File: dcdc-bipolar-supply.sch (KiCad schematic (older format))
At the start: 13 parts

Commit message: swap LT1930A for LT1930 in DCDC bipolar supply
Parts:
- removed U?: LT1930A, Package_SO:MSOP-10_3x3mm_P0.5mm, symbol linear_technology:LT1930A
- added U?: LT1930, Package_SO:MSOP-10_3x3mm_P0.5mm, symbol linear_technology:LT1930
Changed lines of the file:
@@
 Comment4 ""
 $EndDescr
-$Comp
-L linear_technology:LT1930A U?
-U 1 1 5C903C18
-P 4350 3450
-F 0 "U?" H 4350 3600 50  0000 L CNN
-F 1 "LT1930A" H 4200 3500 50  0000 L CNN
-F 2 "Package_SO:MSOP-10_3x3mm_P0.5mm" H 4350 2850 50  0001 C CNN
-F 3 "https://cds.linear.com/docs/en/datasheet/1930a.pdf" H 4450 3400 50  0001 C CNN
-	1    4350 3450
-	1    0    0    -1
-$EndComp
 Text HLabel 3200 3050 0    50   Input ~ 0
 5V_IN
@@
 Connection ~ 3300 3050
 Connection ~ 3700 3050
+$Comp
+L linear_technology:LT1930 U?
+U 1 1 5C87A250
+P 4350 3450
+F 0 "U?" H 4350 3500 50  0000 C CNN
+F 1 "LT1930" H 4350 3600 50  0000 C CNN
+F 2 "Package_SO:MSOP-10_3x3mm_P0.5mm" H 4350 2850 50  0001 C CNN
+F 3 "https://cds.linear.com/docs/en/datasheet/1930a.pdf" H 4450 3400 50  0001 C CNN
+	1    4350 3450
+	1    0    0    -1
+$EndComp
 $EndSCHEMATC

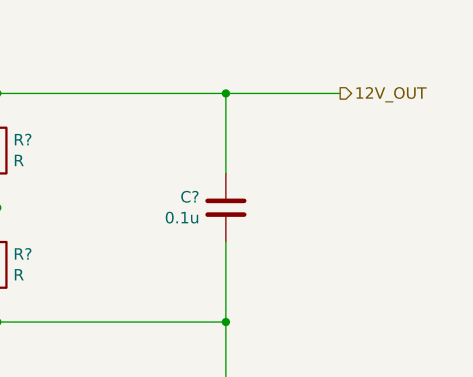
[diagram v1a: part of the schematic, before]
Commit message: add sheets for +/-12V LDOs
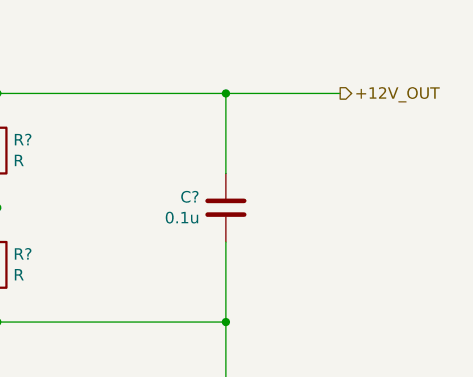
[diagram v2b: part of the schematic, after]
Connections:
- net 12V_OUT renamed +12V_OUT
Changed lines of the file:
@@
 $Descr A4 11693 8268
 encoding utf-8
-Sheet 3 3
+Sheet 3 5
 Title ""
 Date ""
@@
 Connection ~ 6500 3550
 Text HLabel 8000 3050 2    50   Output ~ 0
-12V_OUT
++12V_OUT
 Wire Wire Line
 	6500 3150 6500 3050

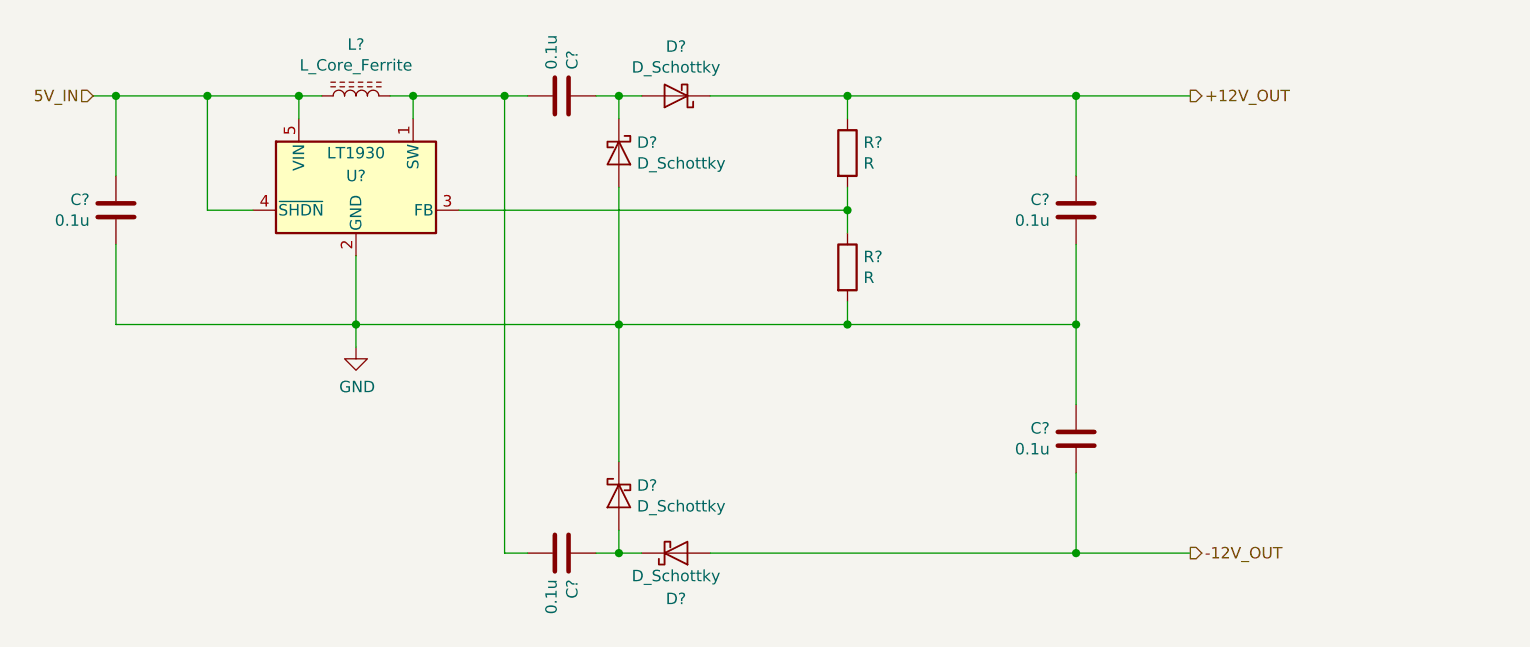
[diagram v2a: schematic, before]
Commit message: update schematic after LTSpice simulations
- enable EN/UV and PGFB usage for LDOs
  - PGFB required for fast startup
  - EN/UV required to allow boost to ramp up
- take care of some TODOs in usbc-power sch
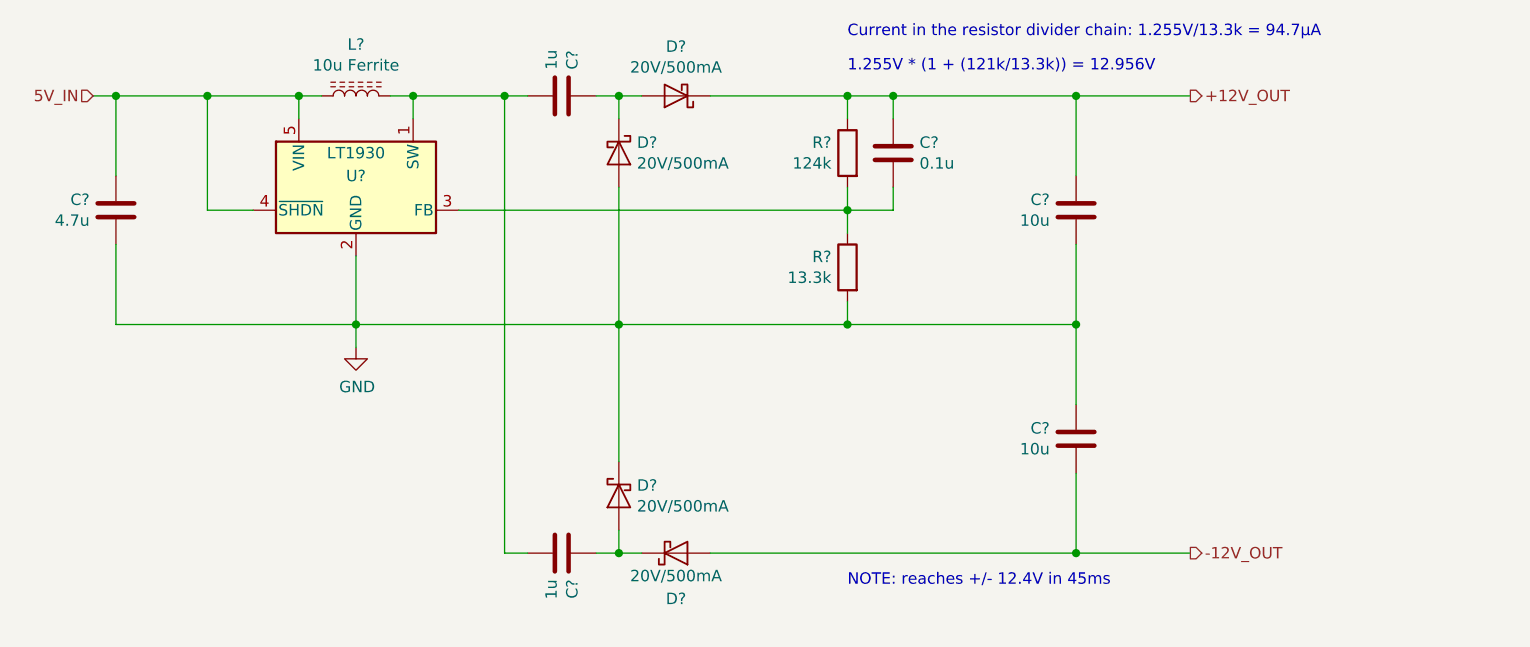
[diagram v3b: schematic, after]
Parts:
- added C?: 0.1u, symbol Device:C
- C?: value 0.1u -> 4.7u
- C? (x2): value 0.1u -> 10u
- C? (x2): value 0.1u -> 1u
- D? (x4): value D_Schottky -> 20V/500mA
- L?: value L_Core_Ferrite -> 10u Ferrite
- R?: value R -> 124k
- R?: value R -> 13.3k
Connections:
- net +12V_OUT: now also C?.2
- net at R?.1, R?.2, U?.3 (FB): now also C?.1
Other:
- note added: "1.255V * (1 + (121k/13.3k)) = 12.956V"
- note added: "Current in the resistor divider chain: 1.255V/13.3k = 94.7µA"
- note added: "NOTE: reaches +/- 12.4V in 45ms"
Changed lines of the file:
@@
 AR Path="/5C903B7C/5C903F02" Ref="C?"  Part="1"
 F 0 "C?" H 3185 3504 50  0000 R CNN
-F 1 "0.1u" H 3185 3595 50  0000 R CNN
+F 1 "4.7u" H 3185 3595 50  0000 R CNN
 F 2 "" H 3338 3400 50  0001 C CNN
 F 3 "" H 3300 3550 50  0001 C CNN
@@
 P 4350 3050
 F 0 "L?" V 4575 3050 50  0000 C CNN
-F 1 "L_Core_Ferrite" V 4484 3050 50  0000 C CNN
+F 1 "10u Ferrite" V 4484 3050 50  0000 C CNN
 F 2 "" H 4350 3050 50  0001 C CNN
 F 3 "~" H 4350 3050 50  0001 C CNN
@@
 P 6500 3300
 F 0 "R?" H 6570 3346 50  0000 L CNN
-F 1 "R" H 6570 3255 50  0000 L CNN
+F 1 "124k" H 6570 3255 50  0000 L CNN
 F 2 "" V 6430 3300 50  0001 C CNN
 F 3 "~" H 6500 3300 50  0001 C CNN
 	1    6500 3300
-	1    0    0    -1
+	-1   0    0    -1
 $EndComp
 $Comp
@@
 P 6500 3800
 F 0 "R?" H 6570 3846 50  0000 L CNN
-F 1 "R" H 6570 3755 50  0000 L CNN
+F 1 "13.3k" H 6570 3755 50  0000 L CNN
 F 2 "" V 6430 3800 50  0001 C CNN
 F 3 "~" H 6500 3800 50  0001 C CNN
 	1    6500 3800
-	1    0    0    -1
+	-1   0    0    -1
 $EndComp
 Wire Wire Line
@@
 	6500 3150 6500 3050
 Wire Wire Line
-	6500 3050 7500 3050
+	6500 3050 6700 3050
 $Comp
 L Device:C C?
@@
 AR Path="/5C903B7C/5C90462E" Ref="C?"  Part="1"
 F 0 "C?" H 7385 3504 50  0000 R CNN
-F 1 "0.1u" H 7385 3595 50  0000 R CNN
+F 1 "10u" H 7385 3595 50  0000 R CNN
 F 2 "" H 7538 3400 50  0001 C CNN
 F 3 "" H 7500 3550 50  0001 C CNN
@@
 P 5500 3300
 F 0 "D?" V 5454 3379 50  0000 L CNN
-F 1 "D_Schottky" V 5545 3379 50  0000 L CNN
+F 1 "20V/500mA" V 5545 3379 50  0000 L CNN
 F 2 "" H 5500 3300 50  0001 C CNN
-F 3 "~" H 5500 3300 50  0001 C CNN
+F 3 "https://www.onsemi.com/pub/Collateral/MBR0520LT1-D.PDF" H 5500 3300 50  0001 C CNN
 	1    5500 3300
 	0    1    1    0
@@
 P 5750 3050
 F 0 "D?" H 5750 2834 50  0000 C CNN
-F 1 "D_Schottky" H 5750 2925 50  0000 C CNN
+F 1 "20V/500mA" H 5750 2925 50  0000 C CNN
 F 2 "" H 5750 3050 50  0001 C CNN
-F 3 "~" H 5750 3050 50  0001 C CNN
+F 3 "https://www.onsemi.com/pub/Collateral/MBR0520LT1-D.PDF" H 5750 3050 50  0001 C CNN
 	1    5750 3050
 	-1   0    0    1
@@
 AR Path="/5C903B7C/5C904E21" Ref="C?"  Part="1"
 F 0 "C?" H 5135 3004 50  0000 R CNN
-F 1 "0.1u" H 5135 3095 50  0000 R CNN
+F 1 "1u" H 5135 3095 50  0000 R CNN
 F 2 "" H 5288 2900 50  0001 C CNN
 F 3 "" H 5250 3050 50  0001 C CNN
@@
 P 5500 4800
 F 0 "D?" V 5454 4721 50  0000 R CNN
-F 1 "D_Schottky" V 5545 4721 50  0000 R CNN
+F 1 "20V/500mA" V 5545 4721 50  0000 R CNN
 F 2 "" H 5500 4800 50  0001 C CNN
-F 3 "~" H 5500 4800 50  0001 C CNN
+F 3 "https://www.onsemi.com/pub/Collateral/MBR0520LT1-D.PDF" H 5500 4800 50  0001 C CNN
 	1    5500 4800
 	0    -1   1    0
@@
 P 5750 5050
 F 0 "D?" H 5750 5250 50  0000 C CNN
-F 1 "D_Schottky" H 5750 5150 50  0000 C CNN
+F 1 "20V/500mA" H 5750 5150 50  0000 C CNN
 F 2 "" H 5750 5050 50  0001 C CNN
-F 3 "~" H 5750 5050 50  0001 C CNN
+F 3 "https://www.onsemi.com/pub/Collateral/MBR0520LT1-D.PDF" H 5750 5050 50  0001 C CNN
 	1    5750 5050
 	1    0    0    1
@@
 AR Path="/5C903B7C/5C905318" Ref="C?"  Part="1"
 F 0 "C?" H 5135 5004 50  0000 R CNN
-F 1 "0.1u" H 5135 5095 50  0000 R CNN
+F 1 "1u" H 5135 5095 50  0000 R CNN
 F 2 "" H 5288 4900 50  0001 C CNN
 F 3 "" H 5250 5050 50  0001 C CNN
@@
 AR Path="/5C903B7C/5C9089A6" Ref="C?"  Part="1"
 F 0 "C?" H 7385 4504 50  0000 R CNN
-F 1 "0.1u" H 7385 4595 50  0000 R CNN
+F 1 "10u" H 7385 4595 50  0000 R CNN
 F 2 "" H 7538 4400 50  0001 C CNN
 F 3 "" H 7500 4550 50  0001 C CNN
@@
 	1    0    0    -1
 $EndComp
+$Comp
+L Device:C C?
+U 1 1 5CA5C6DD
+P 6700 3300
+AR Path="/5C87B3B6/5CA5C6DD" Ref="C?"  Part="1"
+AR Path="/5C903B7C/5CA5C6DD" Ref="C?"  Part="1"
+F 0 "C?" H 6585 3254 50  0000 R CNN
+F 1 "0.1u" H 6585 3345 50  0000 R CNN
+F 2 "" H 6738 3150 50  0001 C CNN
+F 3 "" H 6700 3300 50  0001 C CNN
+	1    6700 3300
+	-1   0    0    1
+$EndComp
+Wire Wire Line
+	6500 3550 6700 3550
+Wire Wire Line
+	6700 3550 6700 3450
+Wire Wire Line
+	6700 3150 6700 3050
+Connection ~ 6700 3050
+Wire Wire Line
+	6700 3050 7500 3050
+Text Notes 6500 2950 0    50   ~ 0
+1.255V * (1 + (121k/13.3k)) = 12.956V
+Text Notes 6500 5200 0    50   ~ 0
+NOTE: reaches +/- 12.4V in 45ms
+Text Notes 6500 2800 0    50   ~ 0
+Current in the resistor divider chain: 1.255V/13.3k = 94.7µA
 $EndSCHEMATC

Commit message: add BOM info for schottky diodes & LT1930
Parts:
- D? (x4): Description (none) -> SCHOTTKY 20V 500MA SOD123; Manufacturer (none) -> ON Semiconductor; Manufacturer Part Number (none) -> MBR0520L; Supplier (none) -> Digi-Key; Supplier Part Number (none) -> MBR0520LCT-ND
- U?: Description (none) -> 1A Step-Up DC/DC Switching Regulator; Manufacturer (none) -> Linear Technology; Manufacturer Part Number (none) -> LT1930ES5#TRPBF; Supplier (none) -> Digi-Key; Supplier Part Number (none) -> LT1930ES5#TRPBFCT-ND
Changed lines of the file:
@@
 F 1 "20V/500mA" V 5545 3379 50  0000 L CNN
 F 2 "" H 5500 3300 50  0001 C CNN
-F 3 "https://www.onsemi.com/pub/Collateral/MBR0520LT1-D.PDF" H 5500 3300 50  0001 C CNN
+F 3 "https://www.onsemi.cn/PowerSolutions/document/MBR0520L-D.pdf" H 5500 3300 50  0001 C CNN
+F 4 "SCHOTTKY 20V 500MA SOD123" H 0   0   50  0001 C CNN "Description"
+F 5 "ON Semiconductor" H 0   0   50  0001 C CNN "Manufacturer"
+F 6 "MBR0520L" H 0   0   50  0001 C CNN "Manufacturer Part Number"
+F 7 "Digi-Key" H 0   0   50  0001 C CNN "Supplier"
+F 8 "MBR0520LCT-ND" H 0   0   50  0001 C CNN "Supplier Part Number"
 	1    5500 3300
 	0    1    1    0
@@
 F 1 "20V/500mA" H 5750 2925 50  0000 C CNN
 F 2 "" H 5750 3050 50  0001 C CNN
-F 3 "https://www.onsemi.com/pub/Collateral/MBR0520LT1-D.PDF" H 5750 3050 50  0001 C CNN
+F 3 "https://www.onsemi.cn/PowerSolutions/document/MBR0520L-D.pdf" H 5750 3050 50  0001 C CNN
+F 4 "SCHOTTKY 20V 500MA SOD123" H 0   0   50  0001 C CNN "Description"
+F 5 "ON Semiconductor" H 0   0   50  0001 C CNN "Manufacturer"
+F 6 "MBR0520L" H 0   0   50  0001 C CNN "Manufacturer Part Number"
+F 7 "Digi-Key" H 0   0   50  0001 C CNN "Supplier"
+F 8 "MBR0520LCT-ND" H 0   0   50  0001 C CNN "Supplier Part Number"
 	1    5750 3050
 	-1   0    0    1
@@
 F 1 "20V/500mA" V 5545 4721 50  0000 R CNN
 F 2 "" H 5500 4800 50  0001 C CNN
-F 3 "https://www.onsemi.com/pub/Collateral/MBR0520LT1-D.PDF" H 5500 4800 50  0001 C CNN
+F 3 "https://www.onsemi.cn/PowerSolutions/document/MBR0520L-D.pdf" H 5500 4800 50  0001 C CNN
+F 4 "SCHOTTKY 20V 500MA SOD123" H 0   0   50  0001 C CNN "Description"
+F 5 "ON Semiconductor" H 0   0   50  0001 C CNN "Manufacturer"
+F 6 "MBR0520L" H 0   0   50  0001 C CNN "Manufacturer Part Number"
+F 7 "Digi-Key" H 0   0   50  0001 C CNN "Supplier"
+F 8 "MBR0520LCT-ND" H 0   0   50  0001 C CNN "Supplier Part Number"
 	1    5500 4800
 	0    -1   1    0
@@
 F 1 "20V/500mA" H 5750 5150 50  0000 C CNN
 F 2 "" H 5750 5050 50  0001 C CNN
-F 3 "https://www.onsemi.com/pub/Collateral/MBR0520LT1-D.PDF" H 5750 5050 50  0001 C CNN
+F 3 "https://www.onsemi.cn/PowerSolutions/document/MBR0520L-D.pdf" H 5750 5050 50  0001 C CNN
+F 4 "SCHOTTKY 20V 500MA SOD123" H 0   0   50  0001 C CNN "Description"
+F 5 "ON Semiconductor" H 0   0   50  0001 C CNN "Manufacturer"
+F 6 "MBR0520L" H 0   0   50  0001 C CNN "Manufacturer Part Number"
+F 7 "Digi-Key" H 0   0   50  0001 C CNN "Supplier"
+F 8 "MBR0520LCT-ND" H 0   0   50  0001 C CNN "Supplier Part Number"
 	1    5750 5050
 	1    0    0    1
@@
 F 2 "Package_SO:MSOP-10_3x3mm_P0.5mm" H 4350 2850 50  0001 C CNN
 F 3 "https://cds.linear.com/docs/en/datasheet/1930a.pdf" H 4450 3400 50  0001 C CNN
+F 4 "1A Step-Up DC/DC Switching Regulator" H 0   0   50  0001 C CNN "Description"
+F 5 "Linear Technology" H 0   0   50  0001 C CNN "Manufacturer"
+F 6 "LT1930ES5#TRPBF" H 0   0   50  0001 C CNN "Manufacturer Part Number"
+F 7 "Digi-Key" H 0   0   50  0001 C CNN "Supplier"
+F 8 "LT1930ES5#TRPBFCT-ND" H 0   0   50  0001 C CNN "Supplier Part Number"
 	1    4350 3450
 	1    0    0    -1

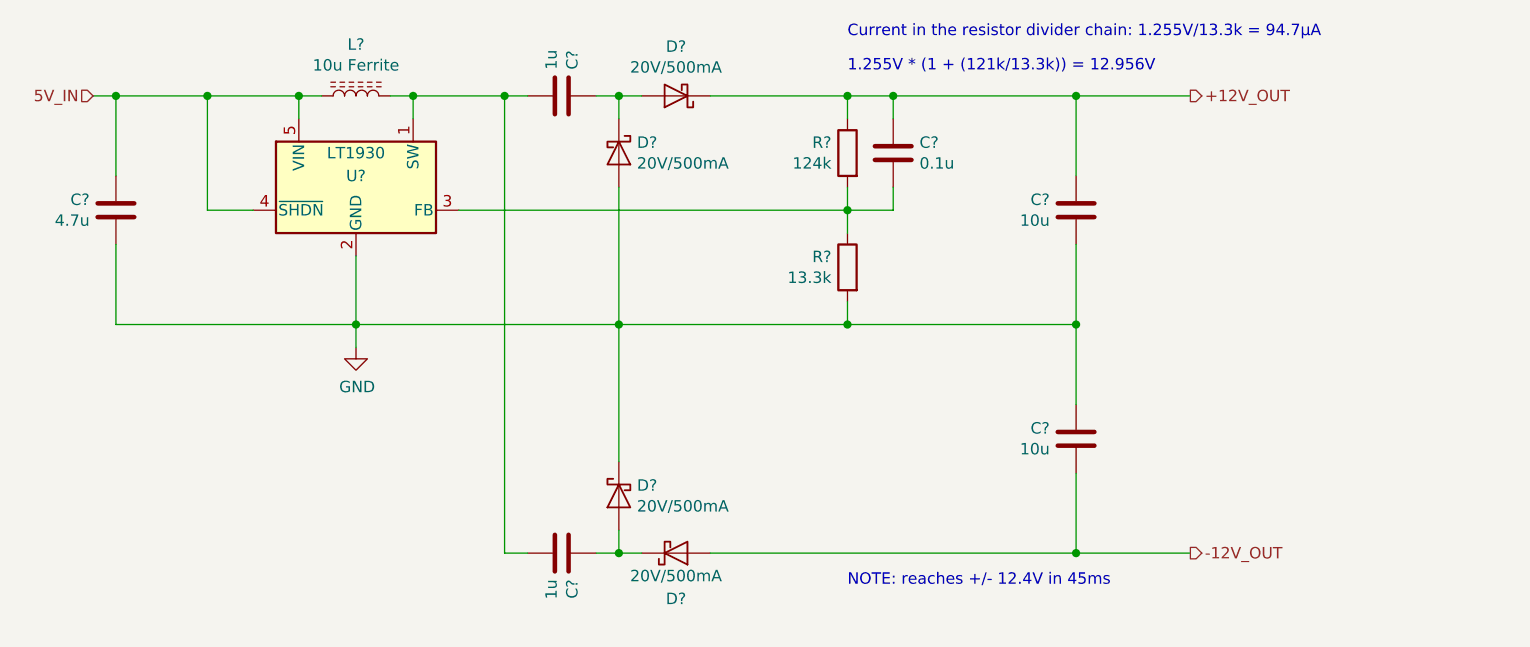
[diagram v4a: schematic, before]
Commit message: update hierarchal pin names to be accurate to new settings
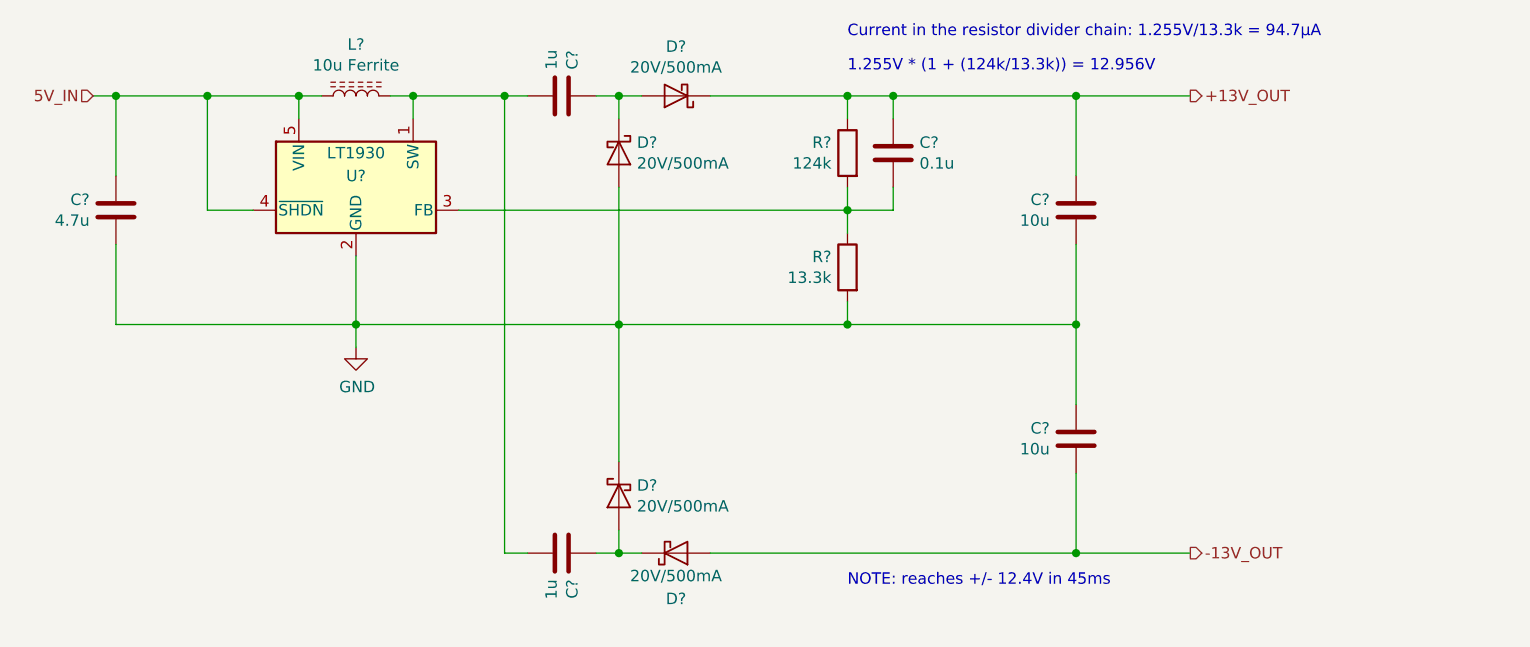
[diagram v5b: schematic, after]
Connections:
- net +12V_OUT renamed +13V_OUT
- net -12V_OUT renamed -13V_OUT
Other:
- note added: "1.255V * (1 + (124k/13.3k)) = 12.956V"
- note removed: "1.255V * (1 + (121k/13.3k)) = 12.956V"
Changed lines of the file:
@@
 Connection ~ 6500 3550
 Text HLabel 8000 3050 2    50   Output ~ 0
-+12V_OUT
++13V_OUT
 Wire Wire Line
 	6500 3150 6500 3050
@@
 Connection ~ 6500 3050
 Text HLabel 8000 5050 2    50   Output ~ 0
--12V_OUT
+-13V_OUT
 Wire Wire Line
 	7500 5050 8000 5050
@@
 	6700 3050 7500 3050
 Text Notes 6500 2950 0    50   ~ 0
-1.255V * (1 + (121k/13.3k)) = 12.956V
+1.255V * (1 + (124k/13.3k)) = 12.956V
 Text Notes 6500 5200 0    50   ~ 0
 NOTE: reaches +/- 12.4V in 45ms

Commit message: BOM details for DC/DC FB resistors
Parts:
- R?: footprint (none) -> Resistor_SMD:R_0805_2012Metric_Pad1.15x1.40mm_HandSolder; Description (none) -> RES SMD 124K OHM 1% 1/8W 0805; Manufacturer (none) -> Panasonic Electronic Components; Manufacturer Part Number (none) -> ERJ-6ENF1243V; Supplier (none) -> Digi-Key; Supplier Part Number (none) -> P124KCCT-ND
- R?: footprint (none) -> Resistor_SMD:R_0805_2012Metric_Pad1.15x1.40mm_HandSolder; Description (none) -> RES SMD 13.3K OHM 1% 1/8W 0805; Manufacturer (none) -> Panasonic Electronic Components; Manufacturer Part Number (none) -> ERJ-6ENF1332V; Supplier (none) -> Digi-Key; Supplier Part Number (none) -> P13.3KCCT-ND
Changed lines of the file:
@@
 F 0 "R?" H 6570 3346 50  0000 L CNN
 F 1 "124k" H 6570 3255 50  0000 L CNN
-F 2 "" V 6430 3300 50  0001 C CNN
-F 3 "~" H 6500 3300 50  0001 C CNN
+F 2 "Resistor_SMD:R_0805_2012Metric_Pad1.15x1.40mm_HandSolder" V 6430 3300 50  0001 C CNN
+F 3 "https://industrial.panasonic.com/cdbs/www-data/pdf/RDA0000/AOA0000C304.pdf" H 6500 3300 50  0001 C CNN
+F 4 "RES SMD 124K OHM 1% 1/8W 0805" H 0   0   50  0001 C CNN "Description"
+F 5 "Panasonic Electronic Components" H 0   0   50  0001 C CNN "Manufacturer"
+F 6 "ERJ-6ENF1243V" H 0   0   50  0001 C CNN "Manufacturer Part Number"
+F 7 "Digi-Key" H 0   0   50  0001 C CNN "Supplier"
+F 8 "P124KCCT-ND" H 0   0   50  0001 C CNN "Supplier Part Number"
 	1    6500 3300
 	-1   0    0    -1
@@
 F 0 "R?" H 6570 3846 50  0000 L CNN
 F 1 "13.3k" H 6570 3755 50  0000 L CNN
-F 2 "" V 6430 3800 50  0001 C CNN
-F 3 "~" H 6500 3800 50  0001 C CNN
+F 2 "Resistor_SMD:R_0805_2012Metric_Pad1.15x1.40mm_HandSolder" V 6430 3800 50  0001 C CNN
+F 3 "https://industrial.panasonic.com/cdbs/www-data/pdf/RDA0000/AOA0000C304.pdf" H 6500 3800 50  0001 C CNN
+F 4 "RES SMD 13.3K OHM 1% 1/8W 0805" H 0   0   50  0001 C CNN "Description"
+F 5 "Panasonic Electronic Components" H 0   0   50  0001 C CNN "Manufacturer"
+F 6 "ERJ-6ENF1332V" H 0   0   50  0001 C CNN "Manufacturer Part Number"
+F 7 "Digi-Key" H 0   0   50  0001 C CNN "Supplier"
+F 8 "P13.3KCCT-ND" H 0   0   50  0001 C CNN "Supplier Part Number"
 	1    6500 3800
 	-1   0    0    -1
